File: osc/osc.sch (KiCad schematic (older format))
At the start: 26 parts, among them P1 CONN_1, P2 CONN_1, P3 CONN_1, P4 CONN_1, P5 CONN_1

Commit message: Reference voltage source is removed (moved to the main board DAC sheet)
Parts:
- removed C? (x2): 0.1, symbol C
- removed K?: CONN_3, symbol CONN_3
- removed R?: 28k, symbol R
- removed R?: 21k, symbol R
- removed U?: ADR280, symbol ADR280
- removed U?: LTC2050, symbol LTC2050
- P4: PartNum (none) -> 3128-1-00-15-00-00-08-0; Vendor (none) -> Mill-Max
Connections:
- net labels removed: Vfb, Vref
- wire segments 66 -> 44
- no-connect marks 2 -> 3
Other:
- note added: "Versatile Clock Generator\nCopyright (c) 2015 Anton Kuzmin\n\nThe VCG is a Free Hardware project, it is released under dual licenses:\n - CERN Open Hardware License (OHL) v1.2\n - Community Research and Academic Programming License (CRAPL)"
- note added: "Vref output\n(not implemented)"
- note removed: "1.2V"
- note removed: "2.8V"
- note removed: "Vref Trim"
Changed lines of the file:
@@
-Vdd
-$Comp
-L CONN_1 P4
-U 1 1 55A7862B
-P 5200 6300
-F 0 "P4" H 5280 6300 40  0000 L CNN
-F 1 "CONN_1" H 5200 6355 30  0001 C CNN
-F 2 "" H 5200 6300 60  0000 C CNN
-F 3 "" H 5200 6300 60  0000 C CNN
-	1    5200 6300
-	1    0    0    1
-$EndComp
-$Comp
-L ADR280 U?
-U 1 1 55F7D740
-P 2550 6250
-F 0 "U?" H 2600 6450 60  0000 C CNN
-F 1 "ADR280" H 2550 6050 60  0000 L CNN
-F 2 "" H 2000 6400 60  0000 C CNN
-F 3 "" H 2000 6400 60  0000 C CNN
-	1    2550 6250
-	1    0    0    -1
-$EndComp
-$Comp
-L LTC2050 U?
-U 1 1 55F7D84F
-P 3700 6300
-F 0 "U?" H 3900 6500 60  0000 C CNN
-F 1 "LTC2050" H 3850 6200 60  0000 L CNN
-F 2 "" H 3700 6300 60  0000 C CNN
-F 3 "" H 3700 6300 60  0000 C CNN
-	1    3700 6300
-	1    0    0    -1
-$EndComp
-$Comp
-L C C?
-U 1 1 55F7D981
-P 2050 6550
-F 0 "C?" H 2050 6650 40  0000 L CNN
-F 1 "0.1" H 2056 6465 40  0000 L CNN
-F 2 "" H 2088 6400 30  0000 C CNN
-F 3 "" H 2050 6550 60  0000 C CNN
-	1    2050 6550
-	1    0    0    -1
-$EndComp
-$Comp
-L C C?
-U 1 1 55F7DA61
-P 3200 6550
-F 0 "C?" H 3200 6650 40  0000 L CNN
-F 1 "0.1" H 3206 6465 40  0000 L CNN
-F 2 "" H 3238 6400 30  0000 C CNN
-F 3 "" H 3200 6550 60  0000 C CNN
-	1    3200 6550
-	1    0    0    -1
-$EndComp
-$Comp
-L R R?
-U 1 1 55F7DAC4
-P 4300 6650
-F 0 "R?" V 4380 6650 40  0000 C CNN
-F 1 "28k" V 4307 6651 40  0000 C CNN
-F 2 "" V 4230 6650 30  0000 C CNN
-F 3 "" H 4300 6650 30  0000 C CNN
-	1    4300 6650
-	-1   0    0    1
-$EndComp
-$Comp
-L R R?
-U 1 1 55F7DB94
-P 4300 7250
-F 0 "R?" V 4380 7250 40  0000 C CNN
-F 1 "21k" V 4307 7251 40  0000 C CNN
-F 2 "" V 4230 7250 30  0000 C CNN
-F 3 "" H 4300 7250 30  0000 C CNN
-	1    4300 7250
-	-1   0    0    1
-$EndComp
-Wire Wire Line
-	2050 5900 2050 6350
-Wire Wire Line
-	2050 6150 2350 6150
-Wire Wire Line
-	2350 6350 2300 6350
-Wire Wire Line
-	2050 5900 3800 5900
-Wire Wire Line
-	3800 5900 3800 6050
-Connection ~ 2050 6150
-Wire Wire Line
-	3100 6250 3500 6250
-Wire Wire Line
-	3200 6350 3200 6250
-Connection ~ 3200 6250
-Wire Wire Line
-	3500 6350 3450 6350
-Wire Wire Line
-	3450 6350 3450 6950
-Wire Wire Line
-	4300 6900 4300 7000
-Wire Wire Line
-	4150 6300 5050 6300
-Wire Wire Line
-	4300 6400 4300 6300
-Connection ~ 4300 6300
-Text Label 4800 6300 0    60   ~ 0
-Vref
-Wire Wire Line
-	2050 6750 2050 7550
-Wire Wire Line
-	2050 7550 4900 7550
-Wire Wire Line
-	4300 7550 4300 7500
-Text Label 2550 7550 0    60   ~ 0
-GND
-Wire Wire Line
-	2300 6350 2300 7550
-Connection ~ 2300 7550
-Wire Wire Line
-	3200 6750 3200 7550
-Connection ~ 3200 7550
-Wire Wire Line
-	3800 6550 3800 7550
-Connection ~ 3800 7550
-$Comp
-L CONN_3 K?
-U 1 1 55F8059C
-P 5250 7450
-F 0 "K?" V 5200 7450 50  0000 C CNN
-F 1 "CONN_3" V 5300 7450 40  0000 C CNN
-F 2 "" H 5250 7450 60  0000 C CNN
-F 3 "" H 5250 7450 60  0000 C CNN
-	1    5250 7450
-	1    0    0    -1
-$EndComp
-Connection ~ 4300 7550
-Wire Wire Line
-	3450 6950 4300 6950
-Connection ~ 4300 6950
-Text Label 4000 6950 0    60   ~ 0
-Vfb
-Wire Wire Line
-	4600 7450 4900 7450
-Text Label 4600 7450 0    60   ~ 0
-Vfb
-Wire Wire Line
-	4900 7350 4750 7350
-Wire Wire Line
-	4750 7350 4750 6300
-Connection ~ 4750 6300
-Text Notes 5050 7250 0    60   ~ 0
-Vref Trim
-Text Notes 3150 6200 0    60   ~ 0
-1.2V
-Text Notes 4350 6250 0    60   ~ 0
-2.8V
-Text Label 2550 5900 0    60   ~ 0
 Vdd
 $Comp
@@
 Text Notes 7300 5700 0    60   ~ 0
 Only one XO should be installed,\nfootprints on the PCB may overlap
+$Comp
+L CONN_1 P4
+U 1 1 5601594E
+P 6050 7450
+F 0 "P4" H 6130 7450 40  0000 L CNN
+F 1 "CONN_1" H 6050 7505 30  0001 C CNN
+F 2 "" H 6050 7450 60  0000 C CNN
+F 3 "" H 6050 7450 60  0000 C CNN
+F 4 "Mill-Max" H 6050 7450 60  0001 C CNN "Vendor"
+F 5 "3128-1-00-15-00-00-08-0" H 6050 7450 60  0001 C CNN "PartNum"
+	1    6050 7450
+	1    0    0    1
+$EndComp
+NoConn ~ 5900 7450
+Text Notes 5900 7350 0    60   ~ 0
+Vref output\n(not implemented)
+Text Notes 7100 7100 0    60   ~ 0
+Versatile Clock Generator\nCopyright (c) 2015 Anton Kuzmin\n\nThe VCG is a Free Hardware project, it is released under dual licenses:\n - CERN Open Hardware License (OHL) v1.2\n - Community Research and Academic Programming License (CRAPL)
 $EndSCHEMATC

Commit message: Draft/Do not use  text is added to the oscillator schematic.
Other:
- note added: "DRAFT DO NOT USE\nThis schematic has not been validated in hardware\nand may contain errors."
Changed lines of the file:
@@
 Text Notes 7100 7100 0    60   ~ 0
 Versatile Clock Generator\nCopyright (c) 2015 Anton Kuzmin\n\nThe VCG is a Free Hardware project, it is released under dual licenses:\n - CERN Open Hardware License (OHL) v1.2\n - Community Research and Academic Programming License (CRAPL)
+Text Notes 7000 6500 0    60   ~ 12
+DRAFT              DO NOT USE\nThis schematic has not been validated in hardware\nand may contain errors.
 $EndSCHEMATC

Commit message: Add load resistor on the control voltage input (Vc)
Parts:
- added R?: 10k, symbol R
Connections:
- wire segments 44 -> 46
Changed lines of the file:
@@
 EESchema Schematic File Version 2
-LIBS:vcg
 LIBS:power
 LIBS:device
@@
 LIBS:contrib
 LIBS:valves
+LIBS:vcg
 LIBS:osc-cache
 EELAYER 25 0
@@
 Wire Wire Line
 	6100 4250 7100 4250
-Text Label 6150 4250 0    60   ~ 0
+Text Label 6250 4250 0    60   ~ 0
 Vc
 Text Notes 7700 7500 0    60   ~ 0
@@
 Text Notes 7000 6500 0    60   ~ 12
 DRAFT              DO NOT USE\nThis schematic has not been validated in hardware\nand may contain errors.
+$Comp
+L R R?
+U 1 1 56409E4E
+P 6200 4600
+F 0 "R?" V 6280 4600 40  0000 C CNN
+F 1 "10k" V 6207 4601 40  0000 C CNN
+F 2 "" V 6130 4600 30  0000 C CNN
+F 3 "" H 6200 4600 30  0000 C CNN
+	1    6200 4600
+	-1   0    0    1
+$EndComp
+Wire Wire Line
+	6200 4350 6200 4250
+Connection ~ 6200 4250
+Wire Wire Line
+	6200 4850 6200 5250
+Connection ~ 6200 5250
 $EndSCHEMATC

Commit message: Annotate schematic
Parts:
- C1: renamed from C?; value 0.1 -> 0.1uF
- C2: renamed from C?; value 10 -> 10uF
- gave numbers to parts that had none: 13
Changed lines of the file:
@@
 $EndComp
 $Comp
-L CONN_5X2 P?
+L CONN_5X2 P6
 U 1 1 557EFB4D
 P 3750 2800
-F 0 "P?" H 3750 3100 60  0000 C CNN
+F 0 "P6" H 3750 3100 60  0000 C CNN
 F 1 "CONN_5X2" V 3750 2800 50  0000 C CNN
 F 2 "" H 3750 2800 60  0000 C CNN
@@
 $EndComp
 $Comp
-L R R?
+L R R1
 U 1 1 557EFBA9
 P 3550 3600
-F 0 "R?" V 3630 3600 40  0000 C CNN
+F 0 "R1" V 3630 3600 40  0000 C CNN
 F 1 "10" V 3557 3601 40  0000 C CNN
 F 2 "" V 3480 3600 30  0000 C CNN
@@
 $EndComp
 $Comp
-L R R?
+L R R2
 U 1 1 557EFC54
 P 3650 3950
-F 0 "R?" V 3730 3950 40  0000 C CNN
+F 0 "R2" V 3730 3950 40  0000 C CNN
 F 1 "10" V 3657 3951 40  0000 C CNN
 F 2 "" V 3580 3950 30  0000 C CNN
@@
 $EndComp
 $Comp
-L R R?
+L R R3
 U 1 1 557EFCC8
 P 3750 3600
-F 0 "R?" V 3830 3600 40  0000 C CNN
+F 0 "R3" V 3830 3600 40  0000 C CNN
 F 1 "10" V 3757 3601 40  0000 C CNN
 F 2 "" V 3680 3600 30  0000 C CNN
@@
 $EndComp
 $Comp
-L R R?
+L R R4
 U 1 1 557EFD0B
 P 3850 3950
-F 0 "R?" V 3930 3950 40  0000 C CNN
+F 0 "R4" V 3930 3950 40  0000 C CNN
 F 1 "10" V 3857 3951 40  0000 C CNN
 F 2 "" V 3780 3950 30  0000 C CNN
@@
 $EndComp
 $Comp
-L R R?
+L R R5
 U 1 1 557EFD39
 P 3950 3600
-F 0 "R?" V 4030 3600 40  0000 C CNN
+F 0 "R5" V 4030 3600 40  0000 C CNN
 F 1 "10" V 3957 3601 40  0000 C CNN
 F 2 "" V 3880 3600 30  0000 C CNN
@@
 	2900 5250 7100 5250
 $Comp
-L C C?
+L C C1
 U 1 1 557F00A8
 P 4850 2650
-F 0 "C?" H 4850 2750 40  0000 L CNN
-F 1 "0.1" H 4856 2565 40  0000 L CNN
+F 0 "C1" H 4850 2750 40  0000 L CNN
+F 1 "0.1uF" H 4856 2565 40  0000 L CNN
 F 2 "" H 4888 2500 30  0000 C CNN
 F 3 "" H 4850 2650 60  0000 C CNN
@@
 1.0
 $Comp
-L JUMPER JP?
+L JUMPER JP1
 U 1 1 557F292B
 P 4450 2350
-F 0 "JP?" H 4450 2500 60  0000 C CNN
+F 0 "JP1" H 4450 2500 60  0000 C CNN
 F 1 "JUMPER" H 4450 2270 40  0000 C CNN
 F 2 "" H 4450 2350 60  0000 C CNN
@@
 Vdd
 $Comp
-L ASOF3S3 Y?
+L ASOF3S3 Y1
 U 1 1 55F810A1
 P 7550 2800
-F 0 "Y?" H 7350 3000 60  0000 C CNN
+F 0 "Y1" H 7350 3000 60  0000 C CNN
 F 1 "ASOF3S3" H 7300 2600 60  0000 L CNN
 F 2 "" H 7300 2950 60  0000 C CNN
@@
 $EndComp
 $Comp
-L AST3TQ-28 Y?
+L AST3TQ-28 Y3
 U 1 1 55F810F8
 P 7550 4350
-F 0 "Y?" H 7350 4550 60  0000 C CNN
+F 0 "Y3" H 7350 4550 60  0000 C CNN
 F 1 "AST3TQ-28" H 7300 4150 60  0000 L CNN
 F 2 "" H 7300 4500 60  0000 C CNN
@@
 $EndComp
 $Comp
-L ASV Y?
+L ASV Y4
 U 1 1 55F811B9
 P 7550 5150
-F 0 "Y?" H 7350 5350 60  0000 C CNN
+F 0 "Y4" H 7350 5350 60  0000 C CNN
 F 1 "ASV" H 7300 4950 60  0000 L CNN
 F 2 "" H 7300 5300 60  0000 C CNN
@@
 NoConn ~ 7200 2700
 $Comp
-L AOCJYR Y?
+L AOCJYR Y2
 U 1 1 55F80A1A
 P 7550 3600
-F 0 "Y?" H 7350 3800 60  0000 C CNN
+F 0 "Y2" H 7350 3800 60  0000 C CNN
 F 1 "AOCJYR" H 7300 3400 60  0000 L CNN
 F 2 "" H 7300 3750 60  0000 C CNN
@@
 NoConn ~ 7200 3500
 $Comp
-L C C?
+L C C2
 U 1 1 55F80AD1
 P 5100 2650
-F 0 "C?" H 5100 2750 40  0000 L CNN
-F 1 "10" H 5106 2565 40  0000 L CNN
+F 0 "C2" H 5100 2750 40  0000 L CNN
+F 1 "10uF" H 5106 2565 40  0000 L CNN
 F 2 "" H 5138 2500 30  0000 C CNN
 F 3 "" H 5100 2650 60  0000 C CNN
@@
 Connection ~ 4850 2350
 $Comp
-L R R?
+L R R7
 U 1 1 55F80C8B
 P 6650 5050
-F 0 "R?" V 6730 5050 40  0000 C CNN
+F 0 "R7" V 6730 5050 40  0000 C CNN
 F 1 "10k" V 6657 5051 40  0000 C CNN
 F 2 "" V 6580 5050 30  0000 C CNN
@@
 DRAFT              DO NOT USE\nThis schematic has not been validated in hardware\nand may contain errors.
 $Comp
-L R R?
+L R R6
 U 1 1 56409E4E
 P 6200 4600
-F 0 "R?" V 6280 4600 40  0000 C CNN
+F 0 "R6" V 6280 4600 40  0000 C CNN
 F 1 "10k" V 6207 4601 40  0000 C CNN
 F 2 "" V 6130 4600 30  0000 C CNN

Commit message: Update schematic to a newer KiCAD version (create rescue library)
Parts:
- C1, C2: symbol C -> C-RESCUE-osc
- R1, R2, R3, R4, R5, R6, R7: symbol R -> R-RESCUE-osc
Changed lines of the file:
@@
 EESchema Schematic File Version 2
+LIBS:osc-rescue
 LIBS:power
 LIBS:device
@@
 LIBS:memory
 LIBS:xilinx
-LIBS:special
 LIBS:microcontrollers
 LIBS:dsp
@@
 $EndComp
 $Comp
-L R R1
+L R-RESCUE-osc R1
 U 1 1 557EFBA9
 P 3550 3600
@@
 $EndComp
 $Comp
-L R R2
+L R-RESCUE-osc R2
 U 1 1 557EFC54
 P 3650 3950
@@
 $EndComp
 $Comp
-L R R3
+L R-RESCUE-osc R3
 U 1 1 557EFCC8
 P 3750 3600
@@
 $EndComp
 $Comp
-L R R4
+L R-RESCUE-osc R4
 U 1 1 557EFD0B
 P 3850 3950
@@
 $EndComp
 $Comp
-L R R5
+L R-RESCUE-osc R5
 U 1 1 557EFD39
 P 3950 3600
@@
 	2900 5250 7100 5250
 $Comp
-L C C1
+L C-RESCUE-osc C1
 U 1 1 557F00A8
 P 4850 2650
@@
 NoConn ~ 7200 3500
 $Comp
-L C C2
+L C-RESCUE-osc C2
 U 1 1 55F80AD1
 P 5100 2650
@@
 Connection ~ 4850 2350
 $Comp
-L R R7
+L R-RESCUE-osc R7
 U 1 1 55F80C8B
 P 6650 5050
@@
 DRAFT              DO NOT USE\nThis schematic has not been validated in hardware\nand may contain errors.
 $Comp
-L R R6
+L R-RESCUE-osc R6
 U 1 1 56409E4E
 P 6200 4600

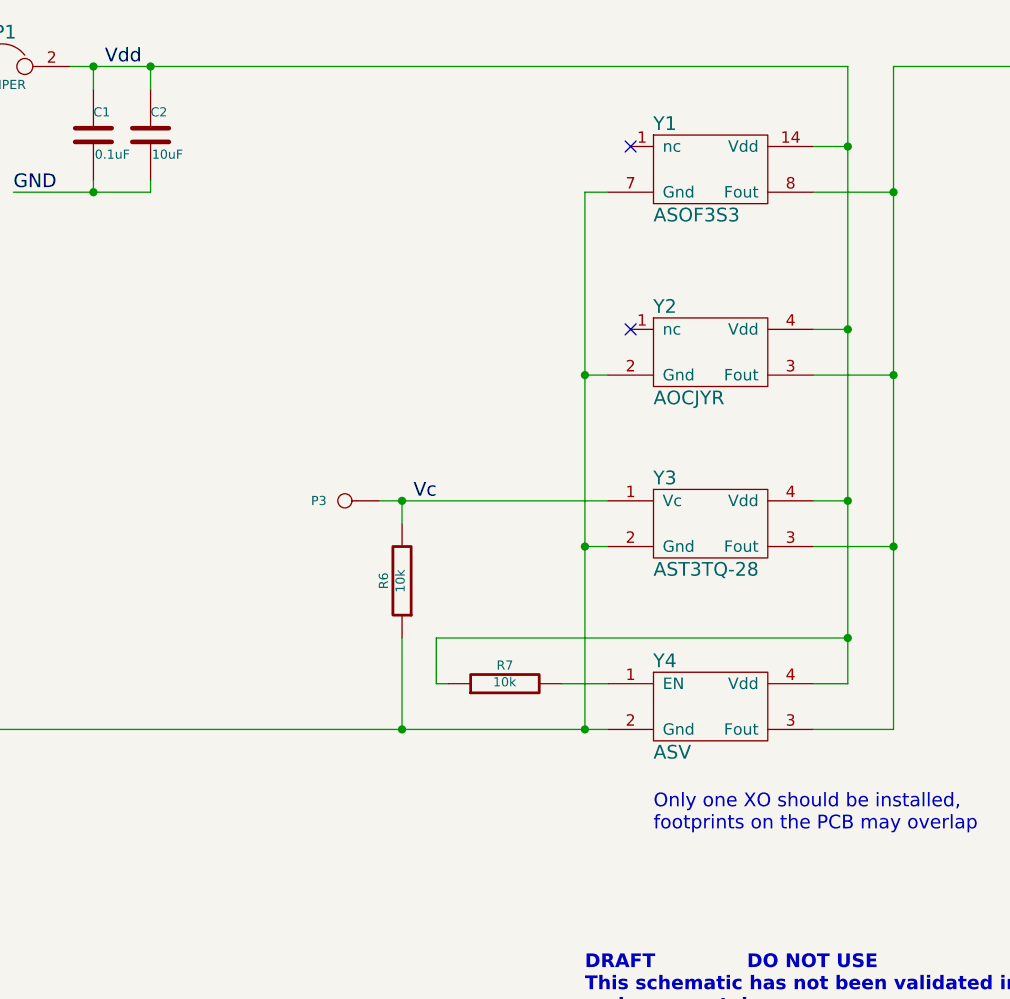
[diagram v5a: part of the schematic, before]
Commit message: Change pull-up/-down and zero-Ohm jumper to accomodate oscillators with different signals on pin 1
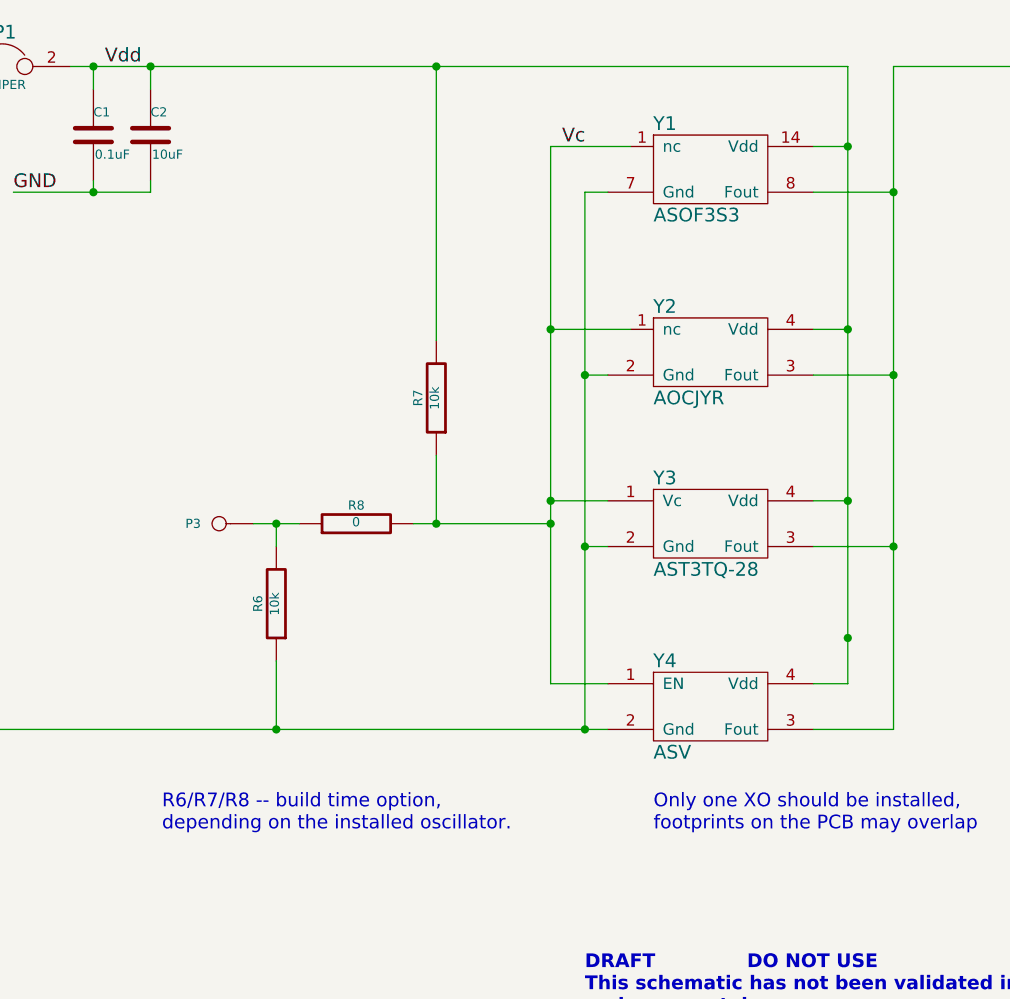
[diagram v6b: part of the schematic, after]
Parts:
- added R8: 0, symbol R-RESCUE-osc
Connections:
- net Vc: now also R7.1, Y1.1 (nc), Y2.1 (nc), Y4.1 (EN), R8.2; no longer P3.1, R6.2
- net Vdd: now also R7.2; no longer R7.1
- new net: P3.1, R6.2, R8.1
- no-connect marks 3 -> 1
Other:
- note added: "R6/R7/R8 -- build time option,\ndepending on the installed oscillator."
- moved on the sheet: P3, R6, R7
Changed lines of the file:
@@
 L CONN_1 P3
 U 1 1 557EFB35
-P 5950 4250
-F 0 "P3" H 6030 4250 40  0000 L CNN
-F 1 "CONN_1" H 5950 4305 30  0001 C CNN
-F 2 "" H 5950 4250 60  0000 C CNN
-F 3 "" H 5950 4250 60  0000 C CNN
-	1    5950 4250
+P 5400 4350
+F 0 "P3" H 5480 4350 40  0000 L CNN
+F 1 "CONN_1" H 5400 4405 30  0001 C CNN
+F 2 "" H 5400 4350 60  0000 C CNN
+F 3 "" H 5400 4350 60  0000 C CNN
+	1    5400 4350
 	-1   0    0    -1
 $EndComp
@@
 Text Label 9000 2350 0    60   ~ 0
 Fout
-Wire Wire Line
-	6100 4250 7100 4250
-Text Label 6250 4250 0    60   ~ 0
+Text Label 6900 2700 0    60   ~ 0
 Vc
 Text Notes 7700 7500 0    60   ~ 0
@@
 	1    0    0    -1
 $EndComp
-NoConn ~ 7200 2700
 $Comp
 L AOCJYR Y2
@@
 	1    0    0    -1
 $EndComp
-NoConn ~ 7200 3500
 $Comp
 L C-RESCUE-osc C2
@@
 L R-RESCUE-osc R7
 U 1 1 55F80C8B
-P 6650 5050
-F 0 "R7" V 6730 5050 40  0000 C CNN
-F 1 "10k" V 6657 5051 40  0000 C CNN
-F 2 "" V 6580 5050 30  0000 C CNN
-F 3 "" H 6650 5050 30  0000 C CNN
-	1    6650 5050
-	0    -1   -1   0
-$EndComp
-Wire Wire Line
-	6900 5050 7100 5050
+P 6350 3800
+F 0 "R7" V 6430 3800 40  0000 C CNN
+F 1 "10k" V 6357 3801 40  0000 C CNN
+F 2 "" V 6280 3800 30  0000 C CNN
+F 3 "" H 6350 3800 30  0000 C CNN
+	1    6350 3800
+	-1   0    0    1
+$EndComp
 Wire Wire Line
 	8150 2350 8150 5050
@@
 	8000 2700 8150 2700
 Connection ~ 8150 2700
-Wire Wire Line
-	6400 5050 6350 5050
-Wire Wire Line
-	6350 5050 6350 4850
-Wire Wire Line
-	6350 4850 8150 4850
 Connection ~ 8150 4850
 Wire Wire Line
@@
 L R-RESCUE-osc R6
 U 1 1 56409E4E
-P 6200 4600
-F 0 "R6" V 6280 4600 40  0000 C CNN
-F 1 "10k" V 6207 4601 40  0000 C CNN
-F 2 "" V 6130 4600 30  0000 C CNN
-F 3 "" H 6200 4600 30  0000 C CNN
-	1    6200 4600
+P 5650 4700
+F 0 "R6" V 5730 4700 40  0000 C CNN
+F 1 "10k" V 5657 4701 40  0000 C CNN
+F 2 "" V 5580 4700 30  0000 C CNN
+F 3 "" H 5650 4700 30  0000 C CNN
+	1    5650 4700
 	-1   0    0    1
 $EndComp
-Wire Wire Line
-	6200 4350 6200 4250
-Connection ~ 6200 4250
-Wire Wire Line
-	6200 4850 6200 5250
-Connection ~ 6200 5250
+$Comp
+L R-RESCUE-osc R8
+U 1 1 56E0C2C0
+P 6000 4350
+F 0 "R8" V 6080 4350 40  0000 C CNN
+F 1 "0" V 6007 4351 40  0000 C CNN
+F 2 "" V 5930 4350 30  0000 C CNN
+F 3 "" H 6000 4350 30  0000 C CNN
+	1    6000 4350
+	0    -1   -1   0
+$EndComp
+Wire Wire Line
+	5550 4350 5750 4350
+Connection ~ 5650 4350
+Wire Wire Line
+	5650 4950 5650 5250
+Connection ~ 5650 5250
+Wire Wire Line
+	6350 3550 6350 2350
+Connection ~ 6350 2350
+Wire Wire Line
+	7200 2700 6850 2700
+Wire Wire Line
+	6850 2700 6850 5050
+Wire Wire Line
+	6850 5050 7100 5050
+Wire Wire Line
+	7100 4250 6850 4250
+Connection ~ 6850 4250
+Wire Wire Line
+	7200 3500 6850 3500
+Connection ~ 6850 3500
+Wire Wire Line
+	5650 4350 5650 4450
+Wire Wire Line
+	6250 4350 6850 4350
+Connection ~ 6850 4350
+Wire Wire Line
+	6350 4050 6350 4350
+Connection ~ 6350 4350
+Text Notes 5150 5700 0    60   ~ 0
+R6/R7/R8 -- build time option,\ndepending on the installed oscillator.
 $EndSCHEMATC
